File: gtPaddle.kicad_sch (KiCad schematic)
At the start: 24 parts, among them IC1 74157N, IC2 74157N, J1 Conn_01x02_Pin, J2 Conn_01x02_Pin, J3 Conn_01x02_Pin, J4 Conn_01x02_Pin, Q1 2N3904, U1 ADC0804LCN

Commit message: Individual headers first pass
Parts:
- removed JP1: PINHD-1X9, gpad1:1X09, symbol gpad1-eagle-import:PINHD-1X9
- added JP1, JP2, JP3, JP4, JP5, JP6, JP7, JP8, JP9: Conn_01x01_Socket, Connector_Wire:SolderWire-0.75sqmm_1x01_D1.25mm_OD2.3mm, symbol Connector:Conn_01x01_Socket
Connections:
- net GND: now also JP8.1 (Pin_1)
- net VCC: now also JP5.1 (Pin_1)
- net at IC1.1 (~{A}/B), IC2.1 (~{A}/B), R12.1: now also JP7.1 (Pin_1)
- net at IC2.4 (1Y): now also JP1.1 (Pin_1)
- net at IC2.7 (2Y): now also JP2.1 (Pin_1)
- net at IC1.4 (1Y): now also JP3.1 (Pin_1)
- net at IC1.7 (2Y): now also JP4.1 (Pin_1)
- net at IC1.9 (3Y): now also JP6.1 (Pin_1)
- net at IC1.12 (4Y): now also JP9.1 (Pin_1)
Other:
- moved on the sheet: C1, C2, C3, C4, C5, IC1A, IC1B, IC2A, IC2B, J1, J2, J3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

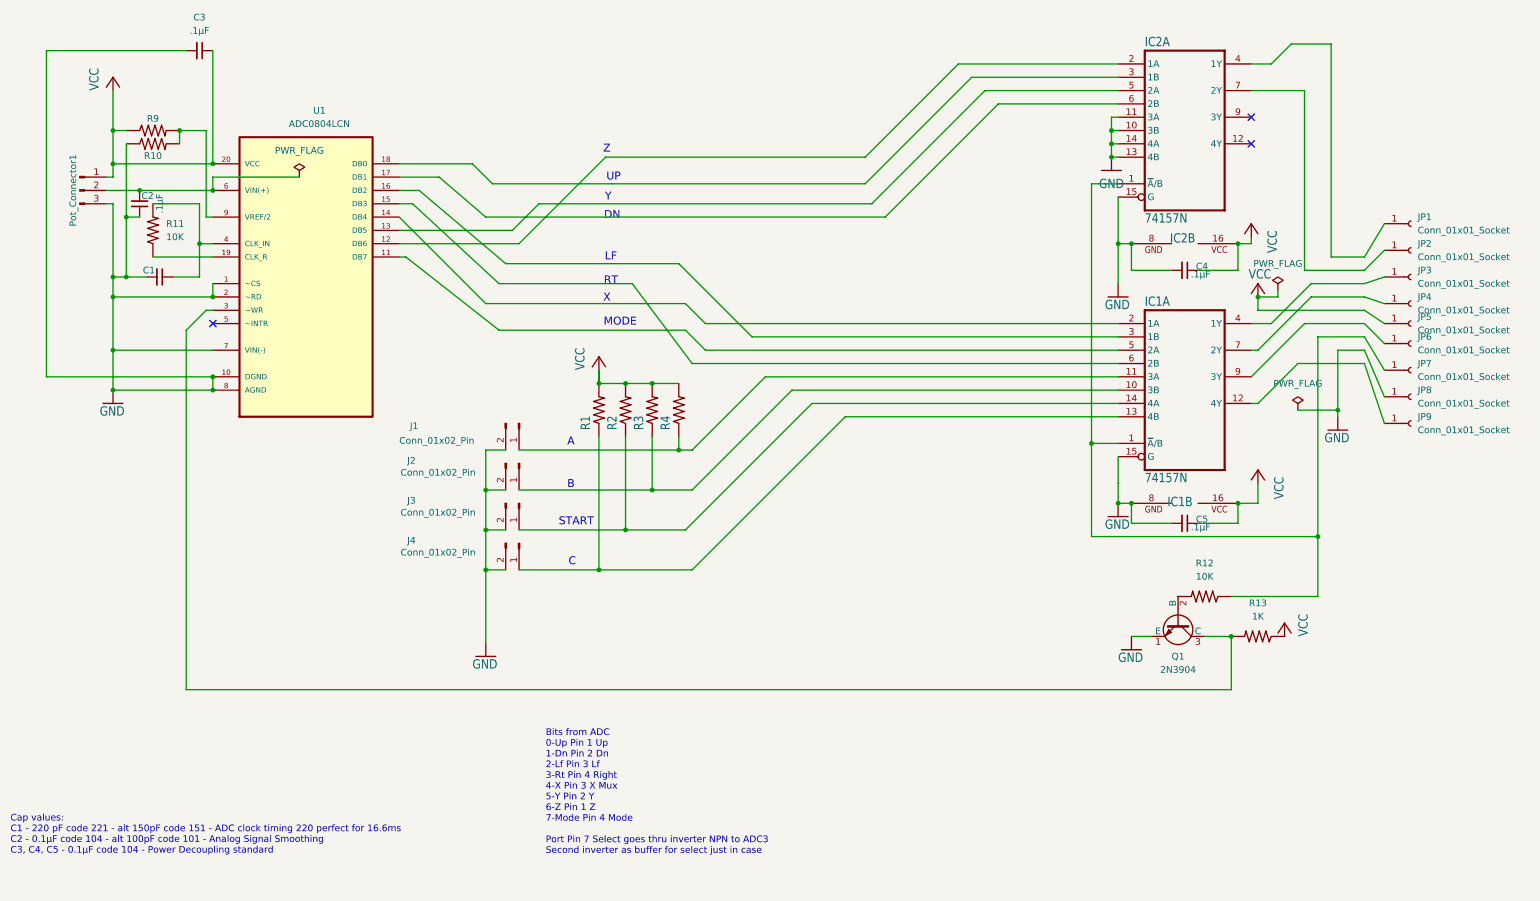
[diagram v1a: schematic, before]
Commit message: add testpoints, ocd edits
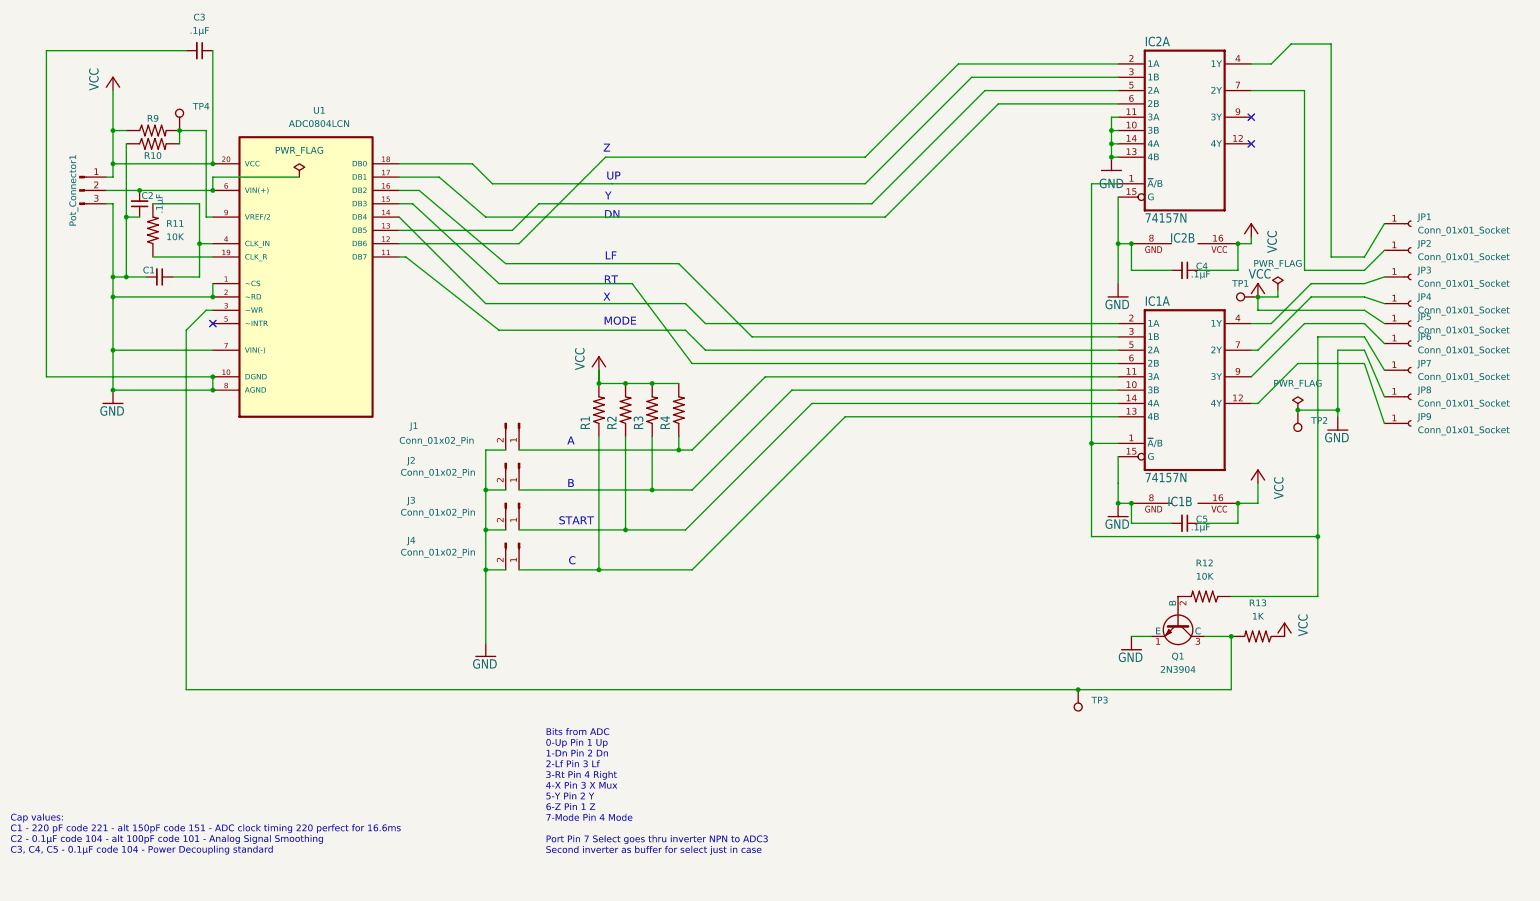
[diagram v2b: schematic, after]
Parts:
- added TP1: VCC, TestPoint:TestPoint_THTPad_D1.5mm_Drill0.7mm, symbol Connector:TestPoint
- added TP2: GND, TestPoint:TestPoint_THTPad_D1.5mm_Drill0.7mm, symbol Connector:TestPoint
- added TP3: INV, TestPoint:TestPoint_THTPad_D1.5mm_Drill0.7mm, symbol Connector:TestPoint
- added TP4: VREF, TestPoint:TestPoint_THTPad_D1.5mm_Drill0.7mm, symbol Connector:TestPoint
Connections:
- net GND: now also TP2.1
- net VCC: now also TP1.1
- net at R10.2, R9.2, U1.9 (VREF/2): now also TP4.1
- net at Q1.3 (C), R13.2, U1.3 (~WR): now also TP3.1

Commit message: added license note to title block
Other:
- title: (none) -> License: TAPR OHL - DKS Interactive LLC
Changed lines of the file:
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@@
 	(generator_version "9.0")
 	(paper "A4")
+	(title_block
+		(title "License: TAPR OHL - DKS Interactive LLC")
+	)
 	(text "UP"
 		(exclude_from_sim no)

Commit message: created hybrid ADC footprint and added to pcb layout
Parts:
- U1: footprint gpad1:DIP254P762X508-20 -> gpad1:ADC0804Hybrid
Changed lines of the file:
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@@
 			)
 		)
-		(property "Footprint" "gpad1:DIP254P762X508-20"
+		(property "Footprint" "gpad1:ADC0804Hybrid"
 			(at 64.77 74.93 0)
 			(effects

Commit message: bigger NPN footprint, better for hand-soldering
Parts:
- Q1: footprint Package_TO_SOT_THT:TO-92S-EBC -> Package_TO_SOT_THT:TO-92_HandSolder
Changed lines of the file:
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@@
 			)
 		)
-		(property "Footprint" "Package_TO_SOT_THT:TO-92S-EBC"
+		(property "Footprint" "Package_TO_SOT_THT:TO-92_HandSolder"
 			(at 229.235 149.86 0)
 			(effects

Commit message: enlarge holes for jst connectors
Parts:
- J1, J2, J3, J4: footprint Connector_JST:JST_PH_B2B-PH-K_1x02_P2.00mm_Vertical -> Connector_JST:JST_PH_B2B-PH-K_1x02_P2.00mm_Vertical_bigHoles
- Pot_Connector1: footprint Connector_JST:JST_PH_B3B-PH-K_1x03_P2.00mm_Vertical -> Connector_JST:JST_PH_B3B-PH-K_1x03_P2.00mm_Vertical_bigHoles
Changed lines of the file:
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@@
 			)
 		)
-		(property "Footprint" "Connector_JST:JST_PH_B2B-PH-K_1x02_P2.00mm_Vertical"
+		(property "Footprint" "Connector_JST:JST_PH_B2B-PH-K_1x02_P2.00mm_Vertical_bigHoles"
 			(at 105.41 129.54 0)
 			(effects
@@
 			)
 		)
-		(property "Footprint" "Connector_JST:JST_PH_B2B-PH-K_1x02_P2.00mm_Vertical"
+		(property "Footprint" "Connector_JST:JST_PH_B2B-PH-K_1x02_P2.00mm_Vertical_bigHoles"
 			(at 105.41 121.92 0)
 			(effects
@@
 			)
 		)
-		(property "Footprint" "Connector_JST:JST_PH_B2B-PH-K_1x02_P2.00mm_Vertical"
+		(property "Footprint" "Connector_JST:JST_PH_B2B-PH-K_1x02_P2.00mm_Vertical_bigHoles"
 			(at 105.41 106.68 0)
 			(effects
@@
 			)
 		)
-		(property "Footprint" "Connector_JST:JST_PH_B2B-PH-K_1x02_P2.00mm_Vertical"
+		(property "Footprint" "Connector_JST:JST_PH_B2B-PH-K_1x02_P2.00mm_Vertical_bigHoles"
 			(at 105.41 114.3 0)
 			(effects
@@
 			)
 		)
-		(property "Footprint" "Connector_JST:JST_PH_B3B-PH-K_1x03_P2.00mm_Vertical"
+		(property "Footprint" "Connector_JST:JST_PH_B3B-PH-K_1x03_P2.00mm_Vertical_bigHoles"
 			(at 21.59 62.23 0)
 			(effects
